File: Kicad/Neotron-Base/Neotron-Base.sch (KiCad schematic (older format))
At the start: 1 part

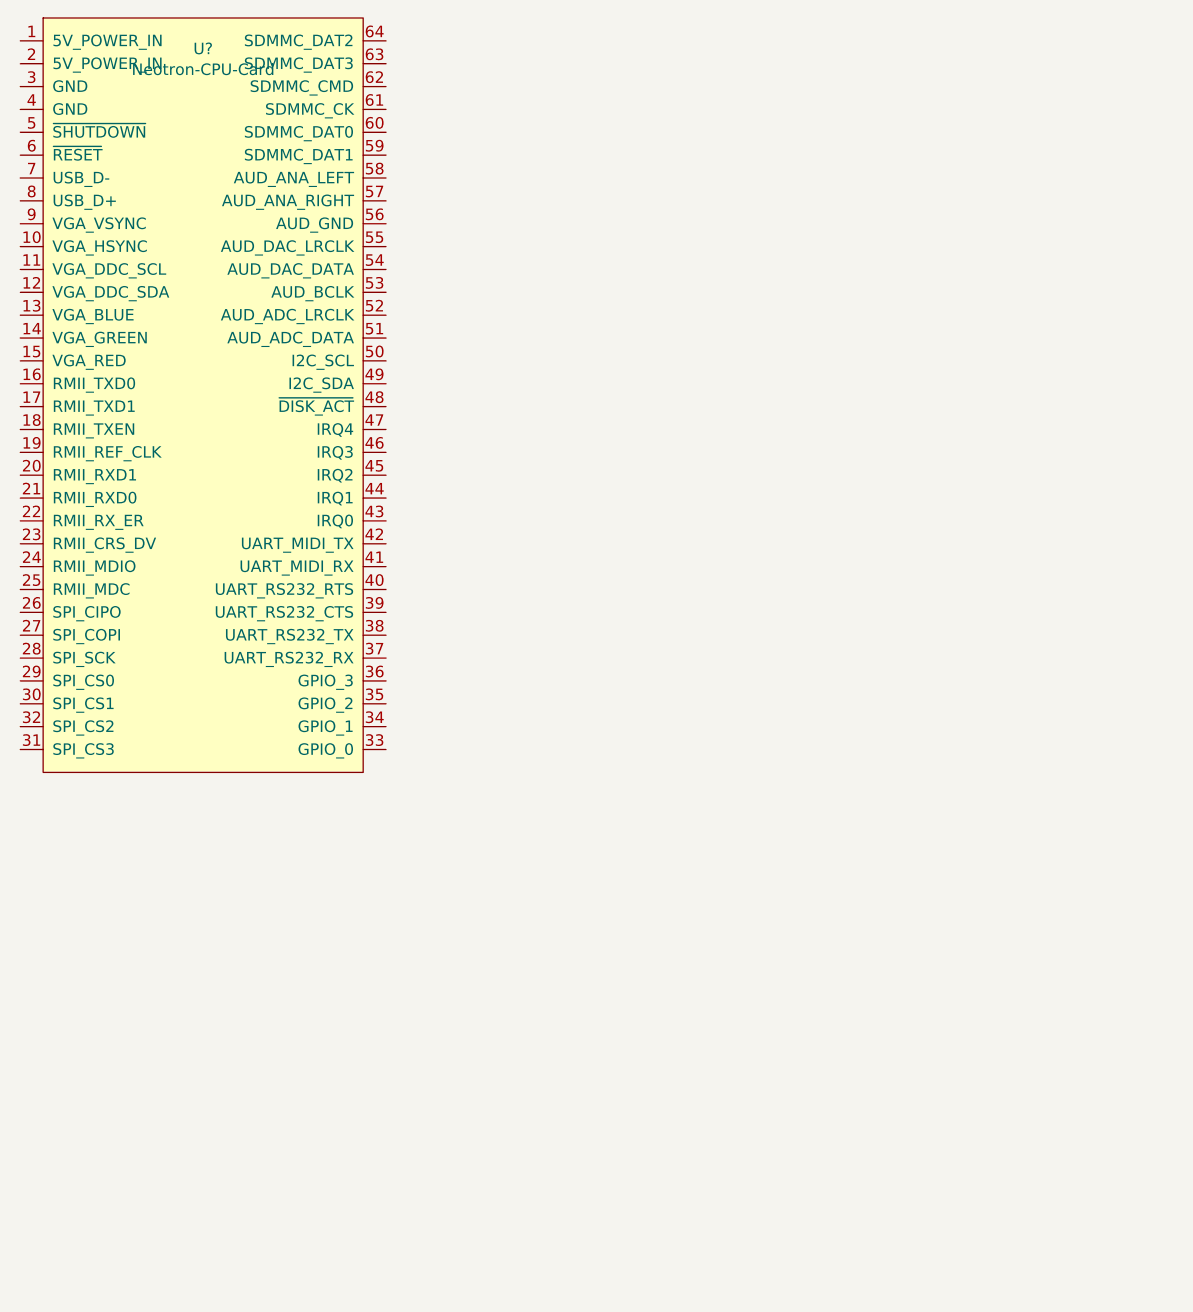
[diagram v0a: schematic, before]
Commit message: Porting over sub-sheets from Neotron 32, and wrote new VGA block.
VGA block uses THS7316 amplifier.
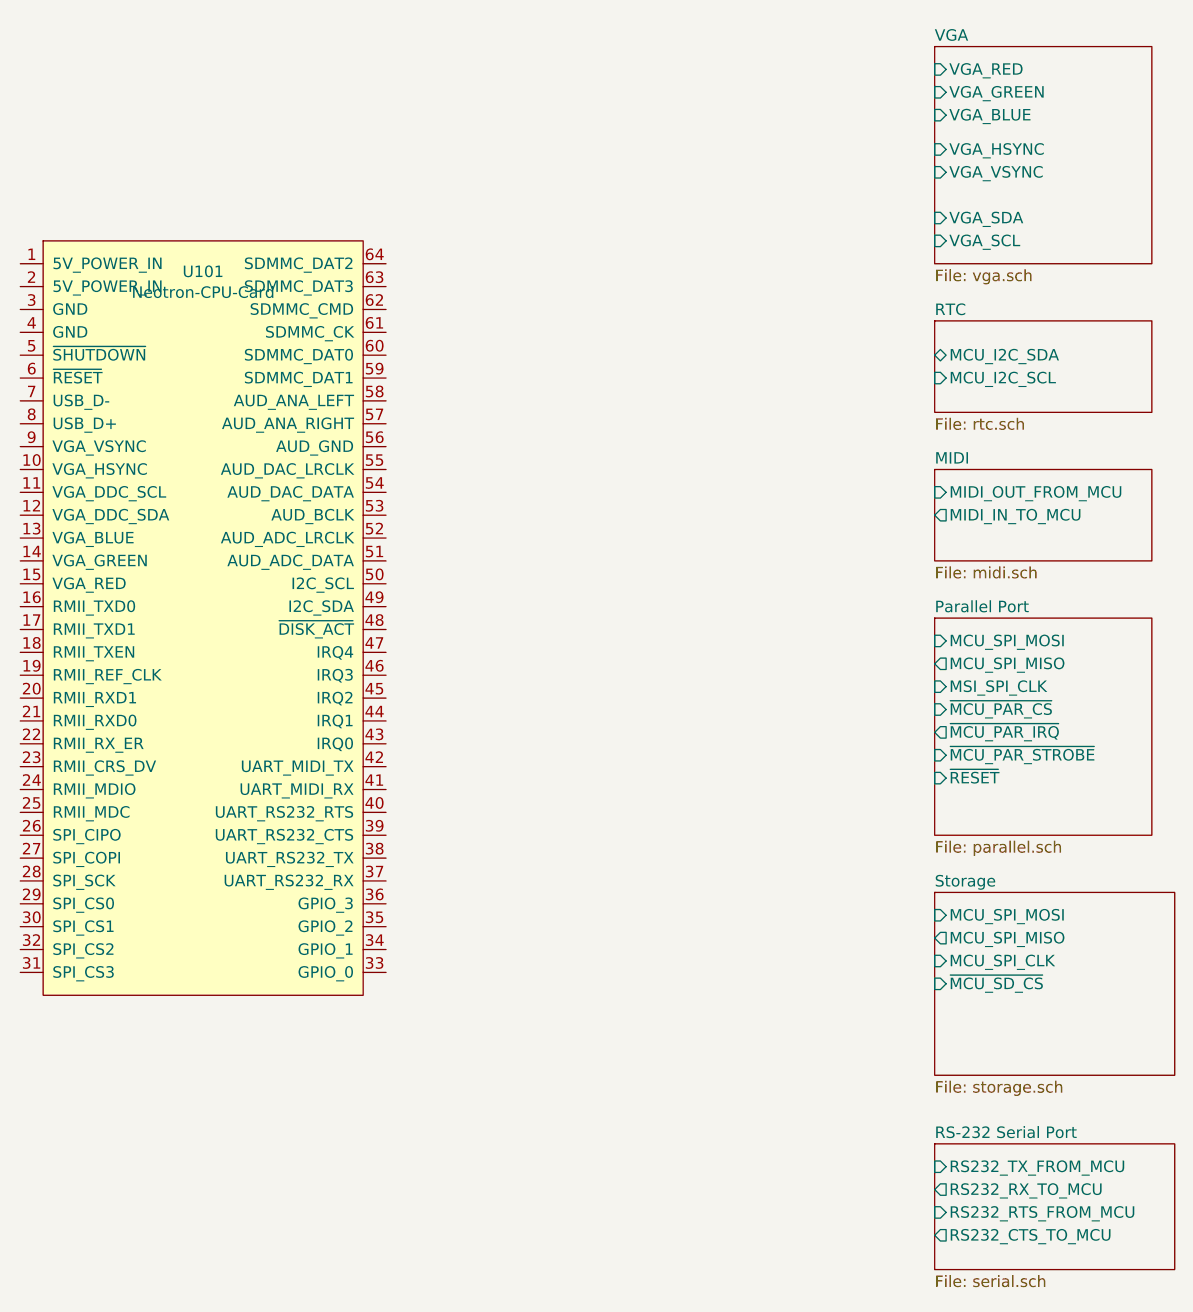
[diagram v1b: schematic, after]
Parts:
- removed U?: Neotron-CPU-Card, symbol Neotron-Base:Neotron-CPU-Card
- added U101: Neotron-CPU-Card, symbol Neotron-Base:Neotron-CPU-Card
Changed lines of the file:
@@
 $Descr A4 11693 8268
 encoding utf-8
-Sheet 1 1
-Title ""
-Date ""
-Rev ""
-Comp ""
-Comment1 ""
-Comment2 ""
+Sheet 1 7
+Title "Neotron Base"
+Date "2020-08-07"
+Rev "[Uncontrolled]"
+Comp "github.com/neotron-compute"
+Comment1 "Copyright (c) Jonathan 'theJPster' Pallant 2020"
+Comment2 "CC BY-SA 4.0"
 Comment3 ""
 Comment4 ""
 $EndDescr
 $Comp
-L Neotron-Base:Neotron-CPU-Card U?
-U 1 1 5F24CF37
-P 5750 2275
-F 0 "U?" H 5750 3740 50  0000 C CNN
-F 1 "Neotron-CPU-Card" H 5750 3649 50  0000 C CNN
-F 2 "" H 4750 3475 50  0001 C CNN
-F 3 "" H 4750 3475 50  0001 C CNN
-	1    5750 2275
+L Neotron-Base:Neotron-CPU-Card U101
+U 1 1 5F2E3825
+P 5750 3250
+F 0 "U101" H 5750 4715 50  0000 C CNN
+F 1 "Neotron-CPU-Card" H 5750 4624 50  0000 C CNN
+F 2 "" H 4750 4450 50  0001 C CNN
+F 3 "" H 4750 4450 50  0001 C CNN
+	1    5750 3250
 	1    0    0    -1
 $EndComp
+$Sheet
+S 8950 800  950  950
+U 5F373616
+F0 "VGA" 50
+F1 "vga.sch" 50
+F2 "VGA_HSYNC" I L 8950 1250 50
+F3 "VGA_VSYNC" I L 8950 1350 50
+F4 "VGA_SDA" I L 8950 1550 50
+F5 "VGA_SCL" I L 8950 1650 50
+F6 "VGA_BLUE" I L 8950 1100 50
+F7 "VGA_GREEN" I L 8950 1000 50
+F8 "VGA_RED" I L 8950 900 50
+$EndSheet
+$Sheet
+S 8950 2000 950  400
+U 5F3C1328
+F0 "RTC" 50
+F1 "rtc.sch" 50
+F2 "MCU_I2C_SDA" B L 8950 2150 50
+F3 "MCU_I2C_SCL" I L 8950 2250 50
+$EndSheet
+$Sheet
+S 8950 2650 950  400
+U 5F3C362C
+F0 "MIDI" 50
+F1 "midi.sch" 50
+F2 "MIDI_OUT_FROM_MCU" I L 8950 2750 50
+F3 "MIDI_IN_TO_MCU" O L 8950 2850 50
+$EndSheet
+$Sheet
+S 8950 3300 950  950
+U 5F3C3642
+F0 "Parallel Port" 50
+F1 "parallel.sch" 50
+F2 "~MCU_PAR_CS" I L 8950 3700 50
+F3 "~MCU_PAR_IRQ" O L 8950 3800 50
+F4 "~MCU_PAR_STROBE" I L 8950 3900 50
+F5 "MCU_SPI_MOSI" I L 8950 3400 50
+F6 "MCU_SPI_MISO" O L 8950 3500 50
+F7 "MSI_SPI_CLK" I L 8950 3600 50
+F8 "~RESET" I L 8950 4000 50
+$EndSheet
+$Sheet
+S 8950 5600 1050 550
+U 5F3C36D1
+F0 "RS-232 Serial Port" 50
+F1 "serial.sch" 50
+F2 "RS232_TX_FROM_MCU" I L 8950 5700 50
+F3 "RS232_RX_TO_MCU" O L 8950 5800 50
+F4 "RS232_RTS_FROM_MCU" I L 8950 5900 50
+F5 "RS232_CTS_TO_MCU" O L 8950 6000 50
+$EndSheet
+$Sheet
+S 8950 4500 1050 800
+U 5F3C3767
+F0 "Storage" 50
+F1 "storage.sch" 50
+F2 "MCU_SPI_MOSI" I L 8950 4600 50
+F3 "MCU_SPI_MISO" O L 8950 4700 50
+F4 "MCU_SPI_CLK" I L 8950 4800 50
+F5 "~MCU_SD_CS" I L 8950 4900 50
+$EndSheet
 $EndSCHEMATC

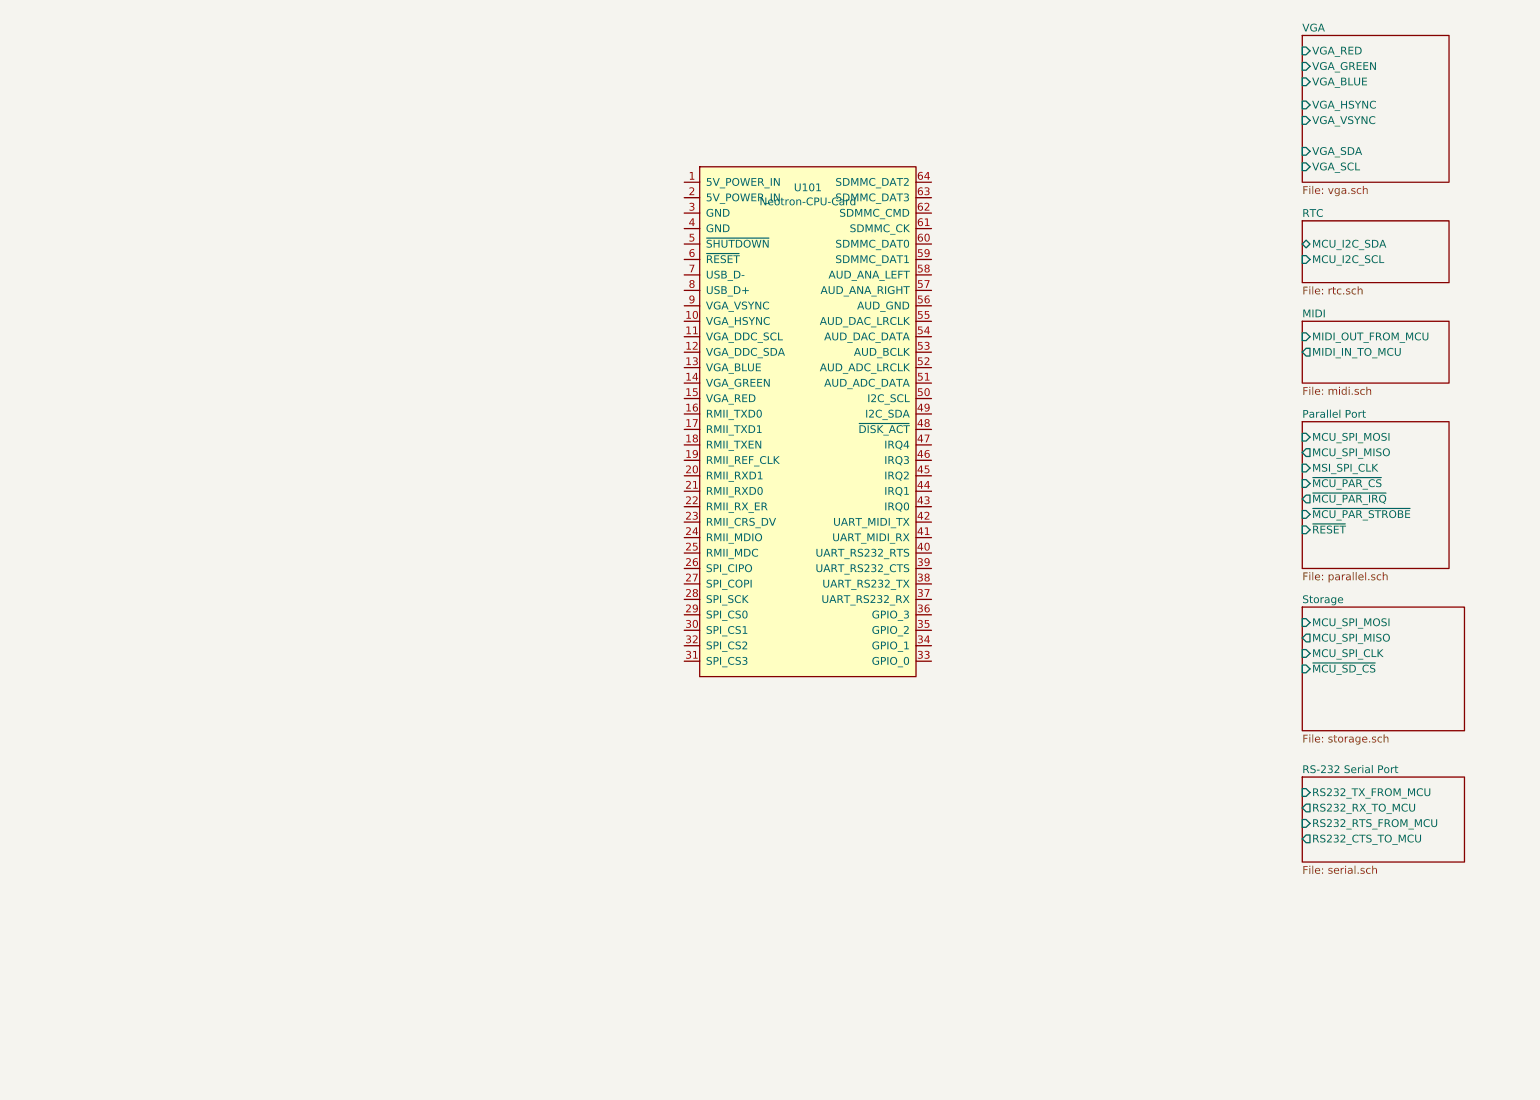
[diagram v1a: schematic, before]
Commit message: Re-work CPU interface to include RMII.
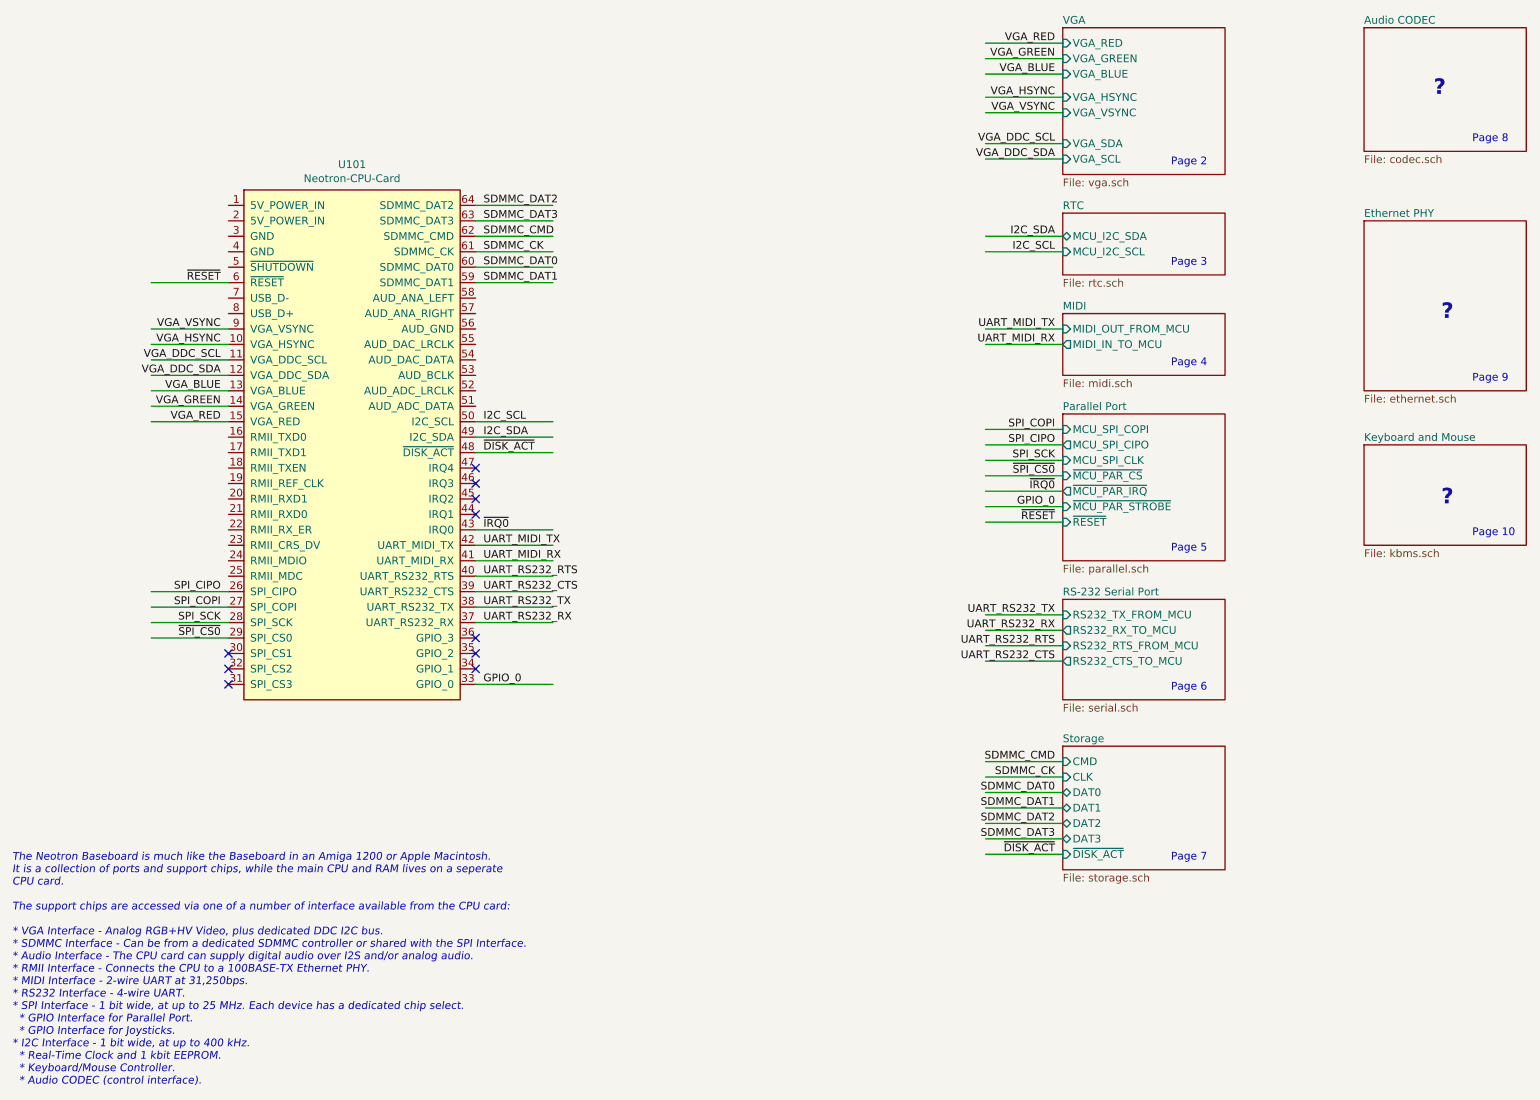
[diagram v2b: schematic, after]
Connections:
- net labels added: GPIO_0, I2C_SCL, I2C_SDA, SDMMC_CK, SDMMC_CMD, SDMMC_DAT0, SDMMC_DAT1, SDMMC_DAT2, SDMMC_DAT3, SPI_CIPO, SPI_COPI, SPI_SCK, UART_MIDI_RX, UART_MIDI_TX, UART_RS232_CTS, UART_RS232_RTS, UART_RS232_RX, UART_RS232_TX, VGA_BLUE, VGA_DDC_SCL, VGA_DDC_SDA, VGA_GREEN, VGA_HSYNC, VGA_RED, VGA_VSYNC, ~DISK_ACT, ~IRQ0, ~RESET, ~SPI_CS0
- wire segments 0 -> 58
- no-connect marks 0 -> 10
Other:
- note added: "?"
- note added: "Page 10"
- note added: "Page 2"
- note added: "Page 3"
- note added: "Page 4"
- note added: "Page 5"
- note added: "Page 6"
- note added: "Page 7"
- note added: "Page 8"
- note added: "Page 9"
- note added: "The Neotron Baseboard is much like the Baseboard in an Amiga 1200 or Apple Macintosh.\nIt is a collection of ports and support chips, while the main CPU and RAM lives on a seperate\nCPU card.\n\nThe support chips are accessed via one of a number of interface available from the CPU card:\n\n* VGA Interface - Analog RGB+HV Video, plus dedicated DDC I2C bus.\n* SDMMC Interface - Can be from a dedica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"
